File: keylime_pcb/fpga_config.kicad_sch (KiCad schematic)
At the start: 5 parts, among them J1 Conn_01x02_Pin, U1 xc7s15cpga196

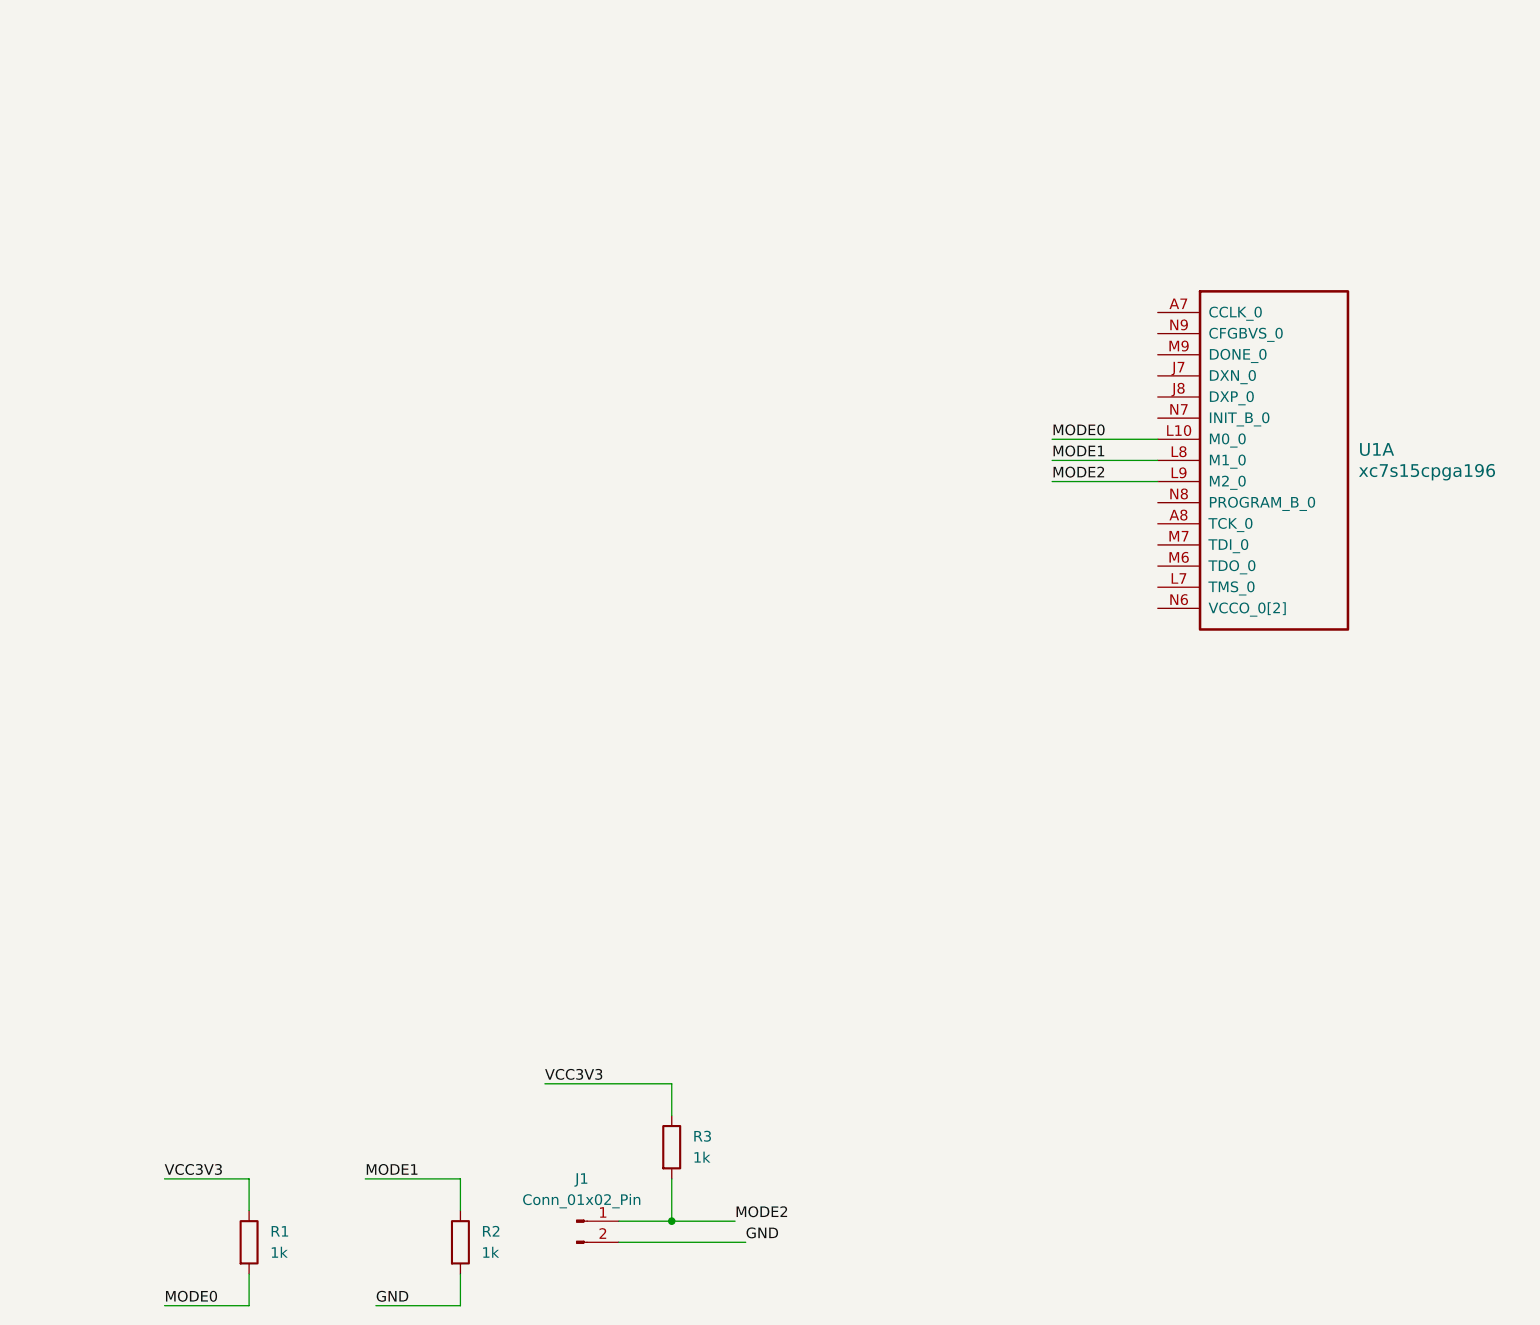
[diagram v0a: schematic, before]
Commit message: Finished adding most components.
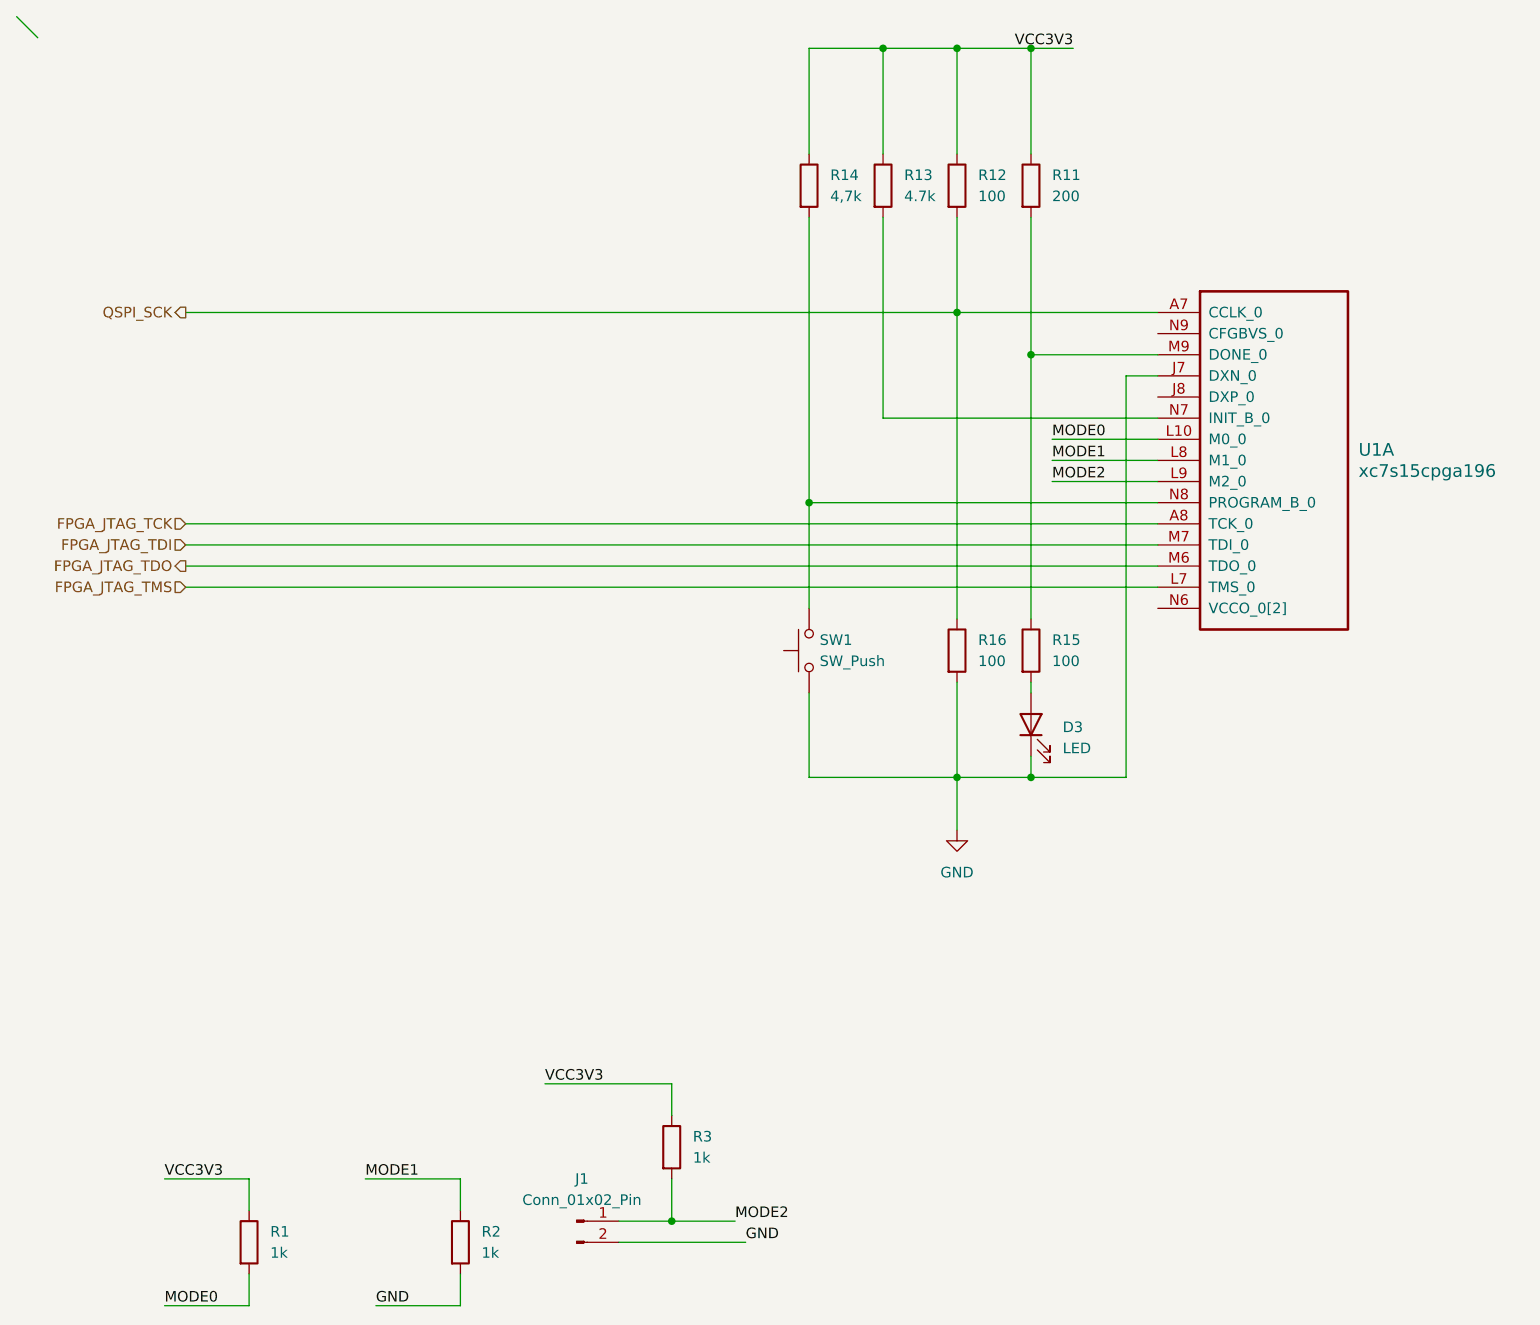
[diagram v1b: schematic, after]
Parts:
- added D3: LED, symbol Device:LED
- added R11: 200, symbol Device:R
- added R12, R15, R16: 100, symbol Device:R
- added R13: 4.7k, symbol Device:R
- added R14: 4,7k, symbol Device:R
- added SW1: SW_Push, symbol Switch:SW_Push
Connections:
- net GND: now also U1.J7 (DXN_0), D3.1 (K), R16.2, SW1.1
- net VCC3V3: now also R11.1, R12.1, R13.1, R14.1
- net QSPI_SCK: now reaches U1.A7 (CCLK_0)
- net QSPI_SCK: now also R12.2, R16.1
- net FPGA_JTAG_TCK: now reaches U1.A8 (TCK_0)
- net FPGA_JTAG_TMS: now reaches U1.L7 (TMS_0)
- net FPGA_JTAG_TDO: now reaches U1.M6 (TDO_0)
- net FPGA_JTAG_TDI: now reaches U1.M7 (TDI_0)
- net at U1.M9 (DONE_0): now also R11.2, R15.1
- net at U1.N7 (INIT_B_0): now also R13.2
- net at U1.N8 (PROGRAM_B_0): now also R14.2, SW1.2
- new net: D3.2 (A), R15.2
